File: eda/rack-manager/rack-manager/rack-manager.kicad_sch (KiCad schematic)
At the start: 49 parts, among them J1 Screw_Terminal_01x02, J10 Conn_01x04_Socket, J11 Conn_01x04_Socket, J12 Conn_01x04_Socket, J13 Conn_01x04_Socket, J14 Conn_01x04_Socket, J2 Screw_Terminal_01x02, J3 Screw_Terminal_01x02, J4 Screw_Terminal_01x02, J5 Screw_Terminal_01x02, J6 Screw_Terminal_01x02, J7 Conn_01x04_Socket, J8 Conn_01x04_Socket, J9 Conn_01x04_Socket, SW1 SW_Push, U1 ADS131M02IRUKR, U2 ADS131M02IRUKR, U3 ADS131M02IRUKR, U5 TCA9548AMRGER

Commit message: Fixed some schematic issues, added gpio expander
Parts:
- added C16, C19: 100nF, symbol Device:C_Small
- added C17, C20: 1uF, symbol Device:C_Small
- added C18: 10uF, symbol Device:C_Small
- added J15, J16: Conn_02x08_Counter_Clockwise, symbol Connector_Generic:Conn_02x08_Counter_Clockwise
- added R15: 100k, symbol Device:R
- added R16: 10k, symbol Device:R
- added U6: PCA9555PW, Package_SO:TSSOP-24_4.4x7.8mm_P0.65mm, symbol Interface_Expansion:PCA9555PW
- C13, C14, C15, C7, C8, C9: value 1nF -> 1uF
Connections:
- net I2C.SCL8 is gone; now on net I2C.SCL7: J10.1 (Pin_1)
- net I2C.SDA8 is gone; now on net I2C.SDA7: J10.2 (Pin_2)
- net +3V3: now also J10.3 (Pin_3), J11.3 (Pin_3), J12.3 (Pin_3), J13.3 (Pin_3), J14.3 (Pin_3), J7.3 (Pin_3), J8.3 (Pin_3), J9.3 (Pin_3), C16.1, C17.1, C18.2, C19.1, C20.1, R15.1, R16.1, U6.24 (VDD)
- net GND: now also C16.2, C17.2, C18.1, C19.2, C20.2, J15.10 (Pin_10), J15.11 (Pin_11), J15.12 (Pin_12), J15.13 (Pin_13), J15.14 (Pin_14), J15.15 (Pin_15), J15.16 (Pin_16), J15.9 (Pin_9), J16.10 (Pin_10), J16.11 (Pin_11), J16.12 (Pin_12), J16.13 (Pin_13), J16.14 (Pin_14), J16.15 (Pin_15), J16.16 (Pin_16), J16.9 (Pin_9), U6.12 (VSS), U6.2 (A1), U6.21 (A0), U6.3 (A2)
- net I2C.SCL6: now also J14.1 (Pin_1)
- net I2C.SCL7: no longer J14.1 (Pin_1)
- net I2C.SDA5: now also J9.2 (Pin_2)
- net I2C.SDA6: now also J14.2 (Pin_2); no longer J9.2 (Pin_2)
- net I2C.SDA7: no longer J14.2 (Pin_2)
- net at U3.10 (CS): now also U4.8 (IO17); no longer U4.22 (IO12)
- net at U1.11 (DRDY), U2.11 (DRDY), U3.11 (DRDY): now also U4.23 (I35), R15.2; no longer U4.19 (I36)
- net at U1.12 (SCLK), U2.12 (SCLK), U3.12 (SCLK): now also U4.22 (IO12); no longer U4.8 (IO17)
- net at R14.2, U4.5 (IO32), U5.19 (SCL): now also U6.22 (SCL)
- net at R13.2, U4.6 (IO33), U5.20 (SDA): now also U6.23 (SDA)
- new net: R16.2, U4.19 (I36), U6.1 (~{INT})
- new net: J16.1 (Pin_1), U6.13 (IO1_0)
- new net: J16.2 (Pin_2), U6.14 (IO1_1)
- new net: J16.3 (Pin_3), U6.15 (IO1_2)
- new net: J16.4 (Pin_4), U6.16 (IO1_3)
- new net: J16.5 (Pin_5), U6.17 (IO1_4)
- new net: J16.6 (Pin_6), U6.18 (IO1_5)
- new net: J16.7 (Pin_7), U6.19 (IO1_6)
- new net: J16.8 (Pin_8), U6.20 (IO1_7)
- new net: J15.1 (Pin_1), U6.4 (IO0_0)
- new net: J15.2 (Pin_2), U6.5 (IO0_1)
- new net: J15.3 (Pin_3), U6.6 (IO0_2)
- new net: J15.4 (Pin_4), U6.7 (IO0_3)
- new net: J15.5 (Pin_5), U6.8 (IO0_4)
- new net: J15.6 (Pin_6), U6.9 (IO0_5)
- new net: J15.7 (Pin_7), U6.10 (IO0_6)
- new net: J15.8 (Pin_8), U6.11 (IO0_7)
- no-connect marks 8 -> 0
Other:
- note added: "3v3 reservoir"
- note added: "A1=A2=A3=0 Addr = 0x20"
- note added: "A1=A2=A3=0 Addr = 0x70"
- note added: "Can't add pullup on CS1 due to IO2 needing to float on boot. To keep it uniform, there are no CS pullups for any of the chips. Instead, we pull them low in software after boot, and then issue a reset to clear any incorrect register values."
- note removed: "A1=A2=A3=0 sets the slave address of the MUX to 0x70"
- moved on the sheet: C1, C10, C11, C12, C13, C2, C3, C4, C5, C6, C7, J1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

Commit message: CAD model for mini ITX mainboard
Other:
- added sheet Analog Front-End (proposed) (analog-front-end.kicad_sch)
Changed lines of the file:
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@@
 		)
 	)
+  (sheet (at 40.0 265.0) (size 55.0 22.0) (fields_autoplaced yes)
+    (stroke (width 0.0006) (type default))
+    (fill (color 0 0 0 0.0000))
+    (property "Sheet name" "Analog Front-End (proposed)" (at 42.54 263.73 0)
+      (effects (font (size 1.27 1.27)) (justify left bottom))
+    )
+    (property "Sheet file" "analog-front-end.kicad_sch" (at 42.54 288.27 0)
+      (effects (font (size 1.27 1.27)) (justify left bottom))
+    )
+  )
 	(sheet_instances
 		(path "/"
 			(page "1")
 		)
-	)
+	    (path "/0c901832-f2ae-4e21-828e-2f1694f3c1c7" (page "2"))
+  )
 	(embedded_fonts no)
 )

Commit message: Rack manager work
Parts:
- added J17: Conn_01x04_Socket, symbol Connector:Conn_01x04_Socket
- added R17, R18, R19, R20, R21, R22, R23, R24, R25, R26, R27, R28, R29, R30, R31, R32: 10k, symbol Device:R
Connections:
- net +3V3: now also J17.3 (Pin_3), R17.1, R18.1, R19.1, R20.1, R21.1, R22.1, R23.1, R24.1, R25.1, R26.1, R27.1, R28.1, R29.1, R30.1, R31.1, R32.1
- net GND: now also J17.4 (Pin_4)
- net I2C.SCL0: now also R17.2
- net I2C.SCL1: now also R26.2
- net I2C.SCL2: now also R20.2
- net I2C.SCL3: now also R28.2
- net I2C.SCL4: now also R22.2
- net I2C.SCL5: now also R30.2
- net I2C.SCL6: now also R24.2
- net I2C.SCL7: now also R32.2
- net I2C.SDA0: now also R18.2
- net I2C.SDA1: now also R25.2
- net I2C.SDA2: now also R19.2
- net I2C.SDA3: now also R27.2
- net I2C.SDA4: now also R21.2
- net I2C.SDA5: now also R29.2
- net I2C.SDA6: now also R23.2
- net I2C.SDA7: now also R31.2
- net at R15.2, U1.11 (DRDY), U4.23 (I35): no longer U2.11 (DRDY), U3.11 (DRDY)
- net at R14.2, U4.5 (IO32), U5.19 (SCL)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: now also J17.1 (Pin_1)
- net at R13.2, U4.6 (IO33), U5.20 (SDA)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: now also J17.2 (Pin_2)
- no-connect marks 0 -> 2
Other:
- removed sheet Analog Front-End (proposed)
- moved on the sheet: C16, C17, R13, R14

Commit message: Board manager work
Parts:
- removed J15, J16: Conn_02x08_Counter_Clockwise, symbol Connector_Generic:Conn_02x08_Counter_Clockwise
- added C1, C2, C27, C28, C3: 100nF, Capacitor_SMD:C_0805_2012Metric, symbol Device:C_Small
- added C29, C30, C31, C4, C5, C6: 10uF, Capacitor_SMD:C_0805_2012Metric, symbol Device:C_Small
- added J10, J3, J6, J9: Screw_Terminal_01x02, TerminalBlock_Phoenix:TerminalBlock_Phoenix_MKDS-1-2-3.81_1x02_P3.81mm_Horizontal, symbol Connector:Screw_Terminal_01x02
- added J11: Conn_02x03_Odd_Even, Connector_IDC:IDC-Header_2x03_P2.54mm_Vertical, symbol Connector_Generic:Conn_02x03_Odd_Even
- added J12: Conn_01x02_Pin, Connector_PinHeader_1.00mm:PinHeader_1x02_P1.00mm_Vertical, symbol Connector:Conn_01x02_Pin
- added J14, J15: Conn_02x06_Counter_Clockwise, Connector_IDC:IDC-Header_2x06_P2.54mm_Vertical, symbol Connector_Generic:Conn_02x06_Counter_Clockwise
- added R15, R16: 1k, Resistor_SMD:R_0805_2012Metric, symbol Device:R
- C10: renamed from C4; footprint (none) -> Capacitor_SMD:C_0805_2012Metric
- C11: renamed from C5; footprint (none) -> Capacitor_SMD:C_0805_2012Metric
- C12: renamed from C6; footprint (none) -> Capacitor_SMD:C_0805_2012Metric
- C13: renamed from C7; footprint (none) -> Capacitor_SMD:C_0805_2012Metric
- C14: renamed from C8; footprint (none) -> Capacitor_SMD:C_0805_2012Metric
- C15: renamed from C9; footprint (none) -> Capacitor_SMD:C_0805_2012Metric
- C16: renamed from C10; footprint (none) -> Capacitor_SMD:C_0805_2012Metric
- C17: renamed from C11; footprint (none) -> Capacitor_SMD:C_0805_2012Metric
- C18: renamed from C12; footprint (none) -> Capacitor_SMD:C_0805_2012Metric
- C19: renamed from C13; footprint (none) -> Capacitor_SMD:C_0805_2012Metric
- C20: renamed from C14; footprint (none) -> Capacitor_SMD:C_0805_2012Metric
- C21: renamed from C15; footprint (none) -> Capacitor_SMD:C_0805_2012Metric
- C22: renamed from C18; footprint (none) -> Capacitor_SMD:C_0805_2012Metric
- C23: renamed from C19; footprint (none) -> Capacitor_SMD:C_0805_2012Metric
- C24: renamed from C20; footprint (none) -> Capacitor_SMD:C_0805_2012Metric
- C25: renamed from C16; footprint (none) -> Capacitor_SMD:C_0805_2012Metric
- C26: renamed from C17; footprint (none) -> Capacitor_SMD:C_0805_2012Metric
- C7: renamed from C1; footprint (none) -> Capacitor_SMD:C_0805_2012Metric
- C8: renamed from C2; footprint (none) -> Capacitor_SMD:C_0805_2012Metric
- C9: renamed from C3; footprint (none) -> Capacitor_SMD:C_0805_2012Metric
- J1, J2: footprint (none) -> TerminalBlock_Phoenix:TerminalBlock_Phoenix_MKDS-1-2-3.81_1x02_P3.81mm_Horizontal; now not fitted
- J13: renamed from J17; footprint (none) -> Connector_JST:JST_XH_B4B-XH-A_1x04_P2.50mm_Vertical; now not fitted
- J16: renamed from J7; footprint (none) -> Connector_JST:JST_XH_B4B-XH-A_1x04_P2.50mm_Vertical; now not fitted
- J17: renamed from J8; footprint (none) -> Connector_JST:JST_XH_B4B-XH-A_1x04_P2.50mm_Vertical; now not fitted
- J18: renamed from J9; footprint (none) -> Connector_JST:JST_XH_B4B-XH-A_1x04_P2.50mm_Vertical; now not fitted
- J19: renamed from J10; footprint (none) -> Connector_JST:JST_XH_B4B-XH-A_1x04_P2.50mm_Vertical; now not fitted
- J20: renamed from J11; footprint (none) -> Connector_JST:JST_XH_B4B-XH-A_1x04_P2.50mm_Vertical; now not fitted
- J21: renamed from J12; footprint (none) -> Connector_JST:JST_XH_B4B-XH-A_1x04_P2.50mm_Vertical; now not fitted
- J22: renamed from J13; footprint (none) -> Connector_JST:JST_XH_B4B-XH-A_1x04_P2.50mm_Vertical; now not fitted
- J23: renamed from J14; footprint (none) -> Connector_JST:JST_XH_B4B-XH-A_1x04_P2.50mm_Vertical; now not fitted
- J4: renamed from J3; footprint (none) -> TerminalBlock_Phoenix:TerminalBlock_Phoenix_MKDS-1-2-3.81_1x02_P3.81mm_Horizontal; now not fitted
- J5: renamed from J4; footprint (none) -> TerminalBlock_Phoenix:TerminalBlock_Phoenix_MKDS-1-2-3.81_1x02_P3.81mm_Horizontal; now not fitted
- J7: renamed from J5; footprint (none) -> TerminalBlock_Phoenix:TerminalBlock_Phoenix_MKDS-1-2-3.81_1x02_P3.81mm_Horizontal; now not fitted
- J8: renamed from J6; footprint (none) -> TerminalBlock_Phoenix:TerminalBlock_Phoenix_MKDS-1-2-3.81_1x02_P3.81mm_Horizontal; now not fitted
- R1, R10, R11, R12, R2, R3, R4, R5, R6, R7, R8, R9: footprint (none) -> Resistor_SMD:R_0805_2012Metric
- R13: renamed from R15; footprint (none) -> Resistor_SMD:R_0805_2012Metric
- R14: renamed from R16; footprint (none) -> Resistor_SMD:R_0805_2012Metric
- R17: renamed from R13; footprint (none) -> Resistor_SMD:R_0805_2012Metric
- R18: renamed from R14; footprint (none) -> Resistor_SMD:R_0805_2012Metric
- R19: renamed from R29; footprint (none) -> Resistor_SMD:R_0805_2012Metric
- R20: renamed from R25; footprint (none) -> Resistor_SMD:R_0805_2012Metric
- R21: renamed from R27; footprint (none) -> Resistor_SMD:R_0805_2012Metric
- R22: renamed from R31; footprint (none) -> Resistor_SMD:R_0805_2012Metric
- R23: renamed from R30; footprint (none) -> Resistor_SMD:R_0805_2012Metric
- R24: renamed from R26; footprint (none) -> Resistor_SMD:R_0805_2012Metric
- R25: renamed from R28; footprint (none) -> Resistor_SMD:R_0805_2012Metric
- R26: renamed from R32; footprint (none) -> Resistor_SMD:R_0805_2012Metric
- R27: renamed from R19; footprint (none) -> Resistor_SMD:R_0805_2012Metric
- R28: renamed from R18; footprint (none) -> Resistor_SMD:R_0805_2012Metric
- R29: renamed from R21; footprint (none) -> Resistor_SMD:R_0805_2012Metric
- R30: renamed from R23; footprint (none) -> Resistor_SMD:R_0805_2012Metric
- R31: renamed from R20; footprint (none) -> Resistor_SMD:R_0805_2012Metric
- R32: renamed from R17; footprint (none) -> Resistor_SMD:R_0805_2012Metric
- R33: renamed from R22; footprint (none) -> Resistor_SMD:R_0805_2012Metric
- R34: renamed from R24; footprint (none) -> Resistor_SMD:R_0805_2012Metric
- SW1: footprint (none) -> Button_Switch_SMD:SW_Push_SPST_NO_Alps_SKRK
- U1, U2, U3: footprint WQFN20_ADS131_TEX -> Package_DFN_QFN:WQFN-20-1EP_3x3mm_P0.4mm_EP1.7x1.7mm
- U4: footprint (none) -> rack-manager:WT32-ETH01; now not fitted
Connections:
- net +3V3: now also C1.2, C2.2, C27.2, C28.2, C29.2, C3.2, C30.2, C31.2, C4.2, C5.2, C6.2, J11.1 (Pin_1), J14.5 (Pin_5), J14.6 (Pin_6), J15.5 (Pin_5), J15.6 (Pin_6), J3.2 (Pin_2), J6.2 (Pin_2), J9.2 (Pin_2)
- net +5V: now also J10.2 (Pin_2)
- net GND: now also U4.14 (GND), U4.23 (GND), C1.1, C2.1, C27.1, C28.1, C29.1, C3.1, C30.1, C31.1, C4.1, C5.1, C6.1, J10.1 (Pin_1), J11.2 (Pin_2), J14.7 (Pin_7), J14.8 (Pin_8), J15.7 (Pin_7), J15.8 (Pin_8), J3.1 (Pin_1), J6.1 (Pin_1), J9.1 (Pin_1), R15.1, R16.1; no longer U4.17 (GND), U4.26 (GND)
- net at C10.1, R8.2: now also U2.3 (AIN1N); no longer U2.4 (AIN1P)
- net at C8.1, R4.2: now also U1.3 (AIN1N); no longer U1.4 (AIN1P)
- net at C8.2, R3.2: now also U1.4 (AIN1P); no longer U1.3 (AIN1N)
- net at C11.2, R9.2: now also U3.2 (AIN0N); no longer U3.1 (AIN0P)
- net at U1.12 (SCLK), U2.12 (SCLK), U3.12 (SCLK): now also U4.18 (IO12); no longer U4.22 (IO12)
- net at U1.13 (DOUT), U2.13 (DOUT), U3.13 (DOUT): now also U4.22 (I39); no longer U4.18 (I39)
- net at U1.15 (CLKIN), U2.15 (CLKIN), U3.15 (CLKIN): now also U4.19 (IO14); no longer U4.21 (IO14)
- net at C11.1, R10.2: now also U3.1 (AIN0P); no longer U3.2 (AIN0N)
- net at C12.2, R11.2: now also U3.4 (AIN1P); no longer U3.3 (AIN1N)
- net at C12.1, R12.2: now also U3.3 (AIN1N); no longer U3.4 (AIN1P)
- net at SW1.2, U4.1 (CLK_EN), U4.4 (ESP32_EN)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: now also J11.3 (Pin_3)
- net at C10.2, R7.2: now also U2.4 (AIN1P); no longer U2.3 (AIN1N)
- net at R13.2, U1.11 (DRDY): now also U4.17 (I35); no longer U4.23 (I35)
- net at U4.13 (Link): now also J12.2 (Pin_2)
- net at U4.15 (IO2): now also U1.10 (CS)
- net at U4.16 (IO4): now also U2.10 (CS)
- net at R14.2, U6.1 (~{INT}): now also U4.21 (I36); no longer U4.19 (I36)
- net at U4.24 (IO0): now also J11.5 (Pin_5); no longer U2.10 (CS)
- net at U4.25 (IO3): now also J11.4 (Pin_4); no longer U1.10 (CS)
- net GPIO10: now reaches U6.13 (IO1_0)
- net GPIO10: now also J14.1 (Pin_1)
- net GPIO11: now reaches U6.14 (IO1_1)
- net GPIO11: now also J14.2 (Pin_2)
- net GPIO12: now reaches U6.15 (IO1_2)
- net GPIO12: now also J14.3 (Pin_3)
- net GPIO13: now reaches U6.16 (IO1_3)
- net GPIO13: now also J14.4 (Pin_4)
- net GPIO14: now reaches U6.17 (IO1_4)
- net GPIO14: now also J14.12 (Pin_12)
- net GPIO15: now reaches U6.18 (IO1_5)
- net GPIO15: now also J14.11 (Pin_11)
- net GPIO16: now reaches U6.19 (IO1_6)
- net GPIO16: now also J14.10 (Pin_10)
- net GPIO17: now reaches U6.20 (IO1_7)
- net GPIO17: now also J14.9 (Pin_9)
- net at C9.1, R6.2: now also U2.1 (AIN0P); no longer U2.2 (AIN0N)
- net at C9.2, R5.2: now also U2.2 (AIN0N); no longer U2.1 (AIN0P)
- net at C7.1, R2.2: now also U1.1 (AIN0P); no longer U1.2 (AIN0N)
- net at C7.2, R1.2: now also U1.2 (AIN0N); no longer U1.1 (AIN0P)
- net GPIO00: now reaches U6.4 (IO0_0)
- net GPIO00: now also J15.1 (Pin_1)
- net GPIO01: now reaches U6.5 (IO0_1)
- net GPIO01: now also J15.2 (Pin_2)
- net GPIO02: now reaches U6.6 (IO0_2)
- net GPIO02: now also J15.3 (Pin_3)
- net GPIO03: now reaches U6.7 (IO0_3)
- net GPIO03: now also J15.4 (Pin_4)
- net GPIO04: now reaches U6.8 (IO0_4)
- net GPIO04: now also J15.12 (Pin_12)
- net GPIO05: now reaches U6.9 (IO0_5)
- net GPIO05: now also J15.11 (Pin_11)
- net GPIO06: now reaches U6.10 (IO0_6)
- net GPIO06: now also J15.10 (Pin_10)
- net GPIO07: now reaches U6.11 (IO0_7)
- net GPIO07: now also J15.9 (Pin_9)
- new net: J11.6 (Pin_6), U4.26 (IO1)
- new net: J12.1 (Pin_1), R15.2, R16.2
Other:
- note removed: "3v3 reservoir"
- moved on the sheet: R17, R18, SW1

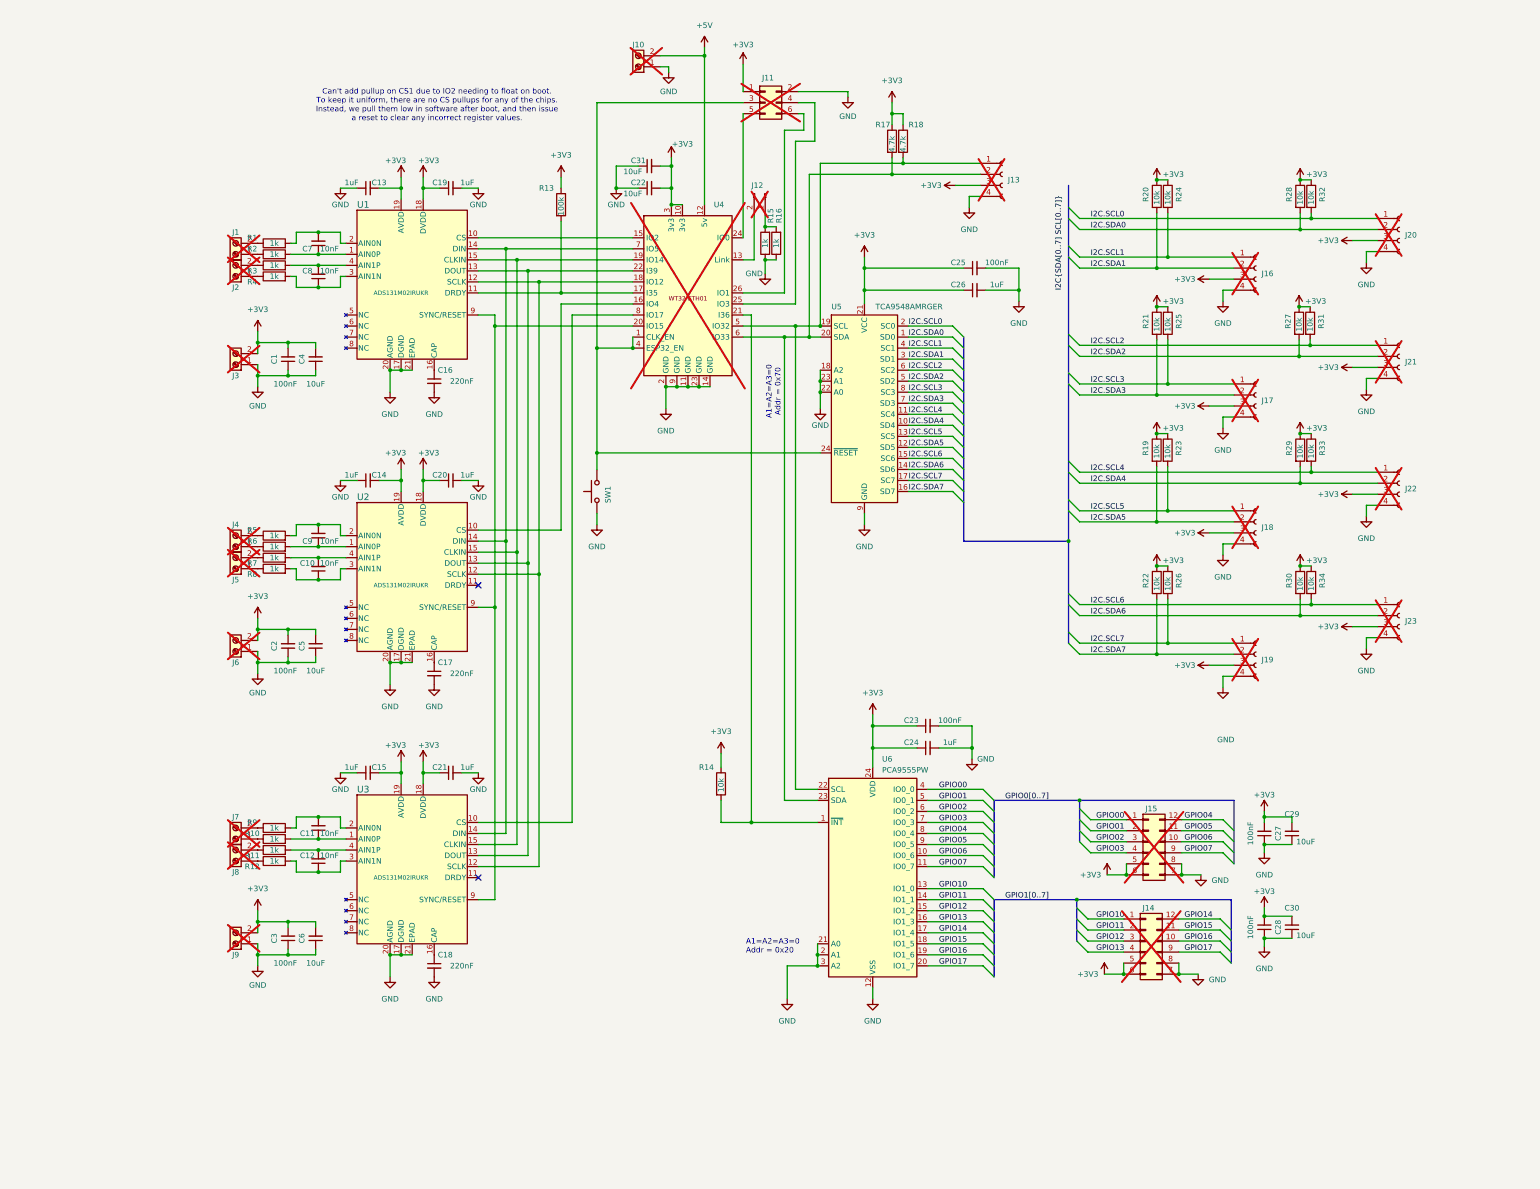
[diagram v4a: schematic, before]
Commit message: Rack manager PCB component placement
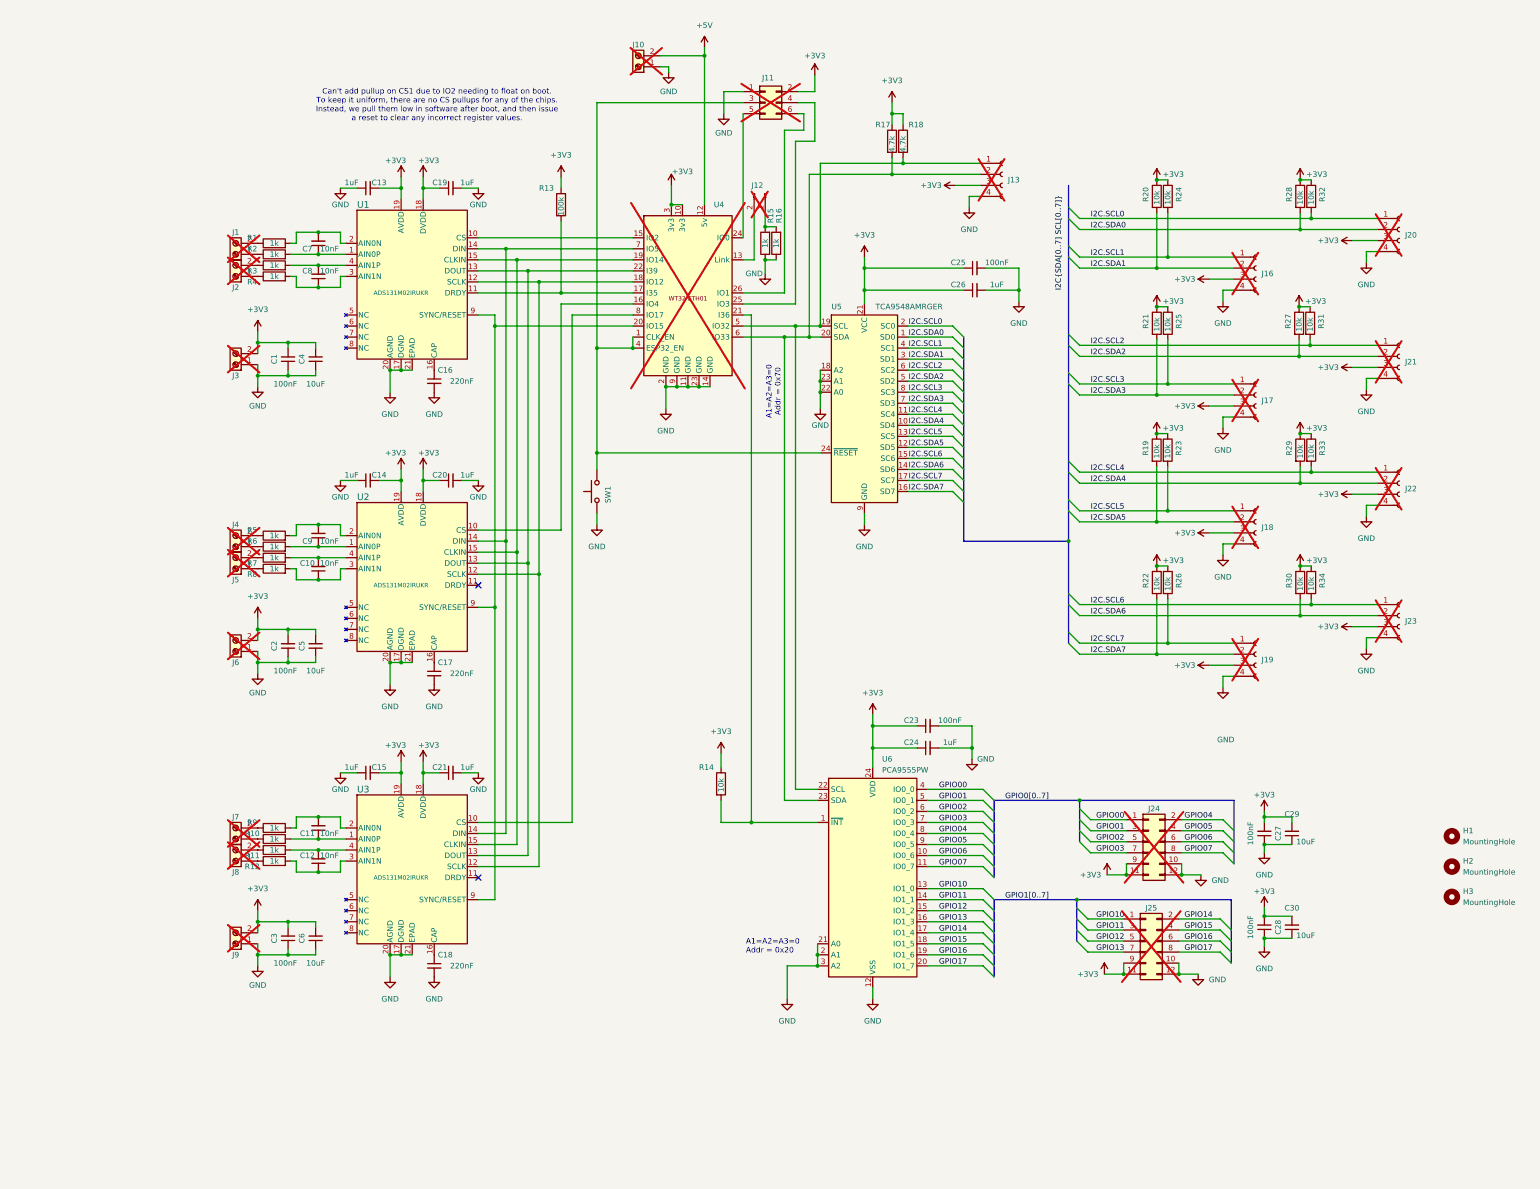
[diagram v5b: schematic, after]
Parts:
- removed C22, C31: 10uF, Capacitor_SMD:C_0805_2012Metric, symbol Device:C_Small
- removed J14, J15: Conn_02x06_Counter_Clockwise, Connector_IDC:IDC-Header_2x06_P2.54mm_Vertical, symbol Connector_Generic:Conn_02x06_Counter_Clockwise
- added H1, H2, H3: MountingHole, MountingHole:MountingHole_4.3mm_M4_ISO14580_Pad_TopBottom, symbol Mechanical:MountingHole
- added J24, J25: Conn_02x06_Odd_Even, Connector_IDC:IDC-Header_2x06_P2.54mm_Vertical, symbol Connector_Generic:Conn_02x06_Odd_Even
- C1, C2, C23, C25, C27, C28, C3: footprint Capacitor_SMD:C_0805_2012Metric -> Capacitor_SMD:C_0603_1608Metric; LCSC (none) -> C14663
- C10, C11, C12, C7, C8, C9: footprint Capacitor_SMD:C_0805_2012Metric -> Capacitor_SMD:C_0603_1608Metric; LCSC (none) -> C57112
- C13, C14, C15, C19, C20, C21, C24, C26: footprint Capacitor_SMD:C_0805_2012Metric -> Capacitor_SMD:C_0603_1608Metric; LCSC (none) -> C15849
- C16, C17, C18: footprint Capacitor_SMD:C_0805_2012Metric -> Capacitor_SMD:C_0603_1608Metric; LCSC (none) -> C21120
- C29, C30, C4, C5, C6: footprint Capacitor_SMD:C_0805_2012Metric -> Capacitor_SMD:C_0603_1608Metric; LCSC (none) -> C19702
- R1, R10, R11, R12, R15, R16, R2, R3, R4, R5, R6, R7, R8, R9: footprint Resistor_SMD:R_0805_2012Metric -> Resistor_SMD:R_0603_1608Metric; LCSC (none) -> C21190
- R13: footprint Resistor_SMD:R_0805_2012Metric -> Resistor_SMD:R_0603_1608Metric; LCSC (none) -> C25803
- R14, R19, R20, R21, R22, R23, R24, R25, R26, R27, R28, R29, R30, R31, R32, R33, R34: footprint Resistor_SMD:R_0805_2012Metric -> Resistor_SMD:R_0603_1608Metric; LCSC (none) -> C25804
- R17, R18: footprint Resistor_SMD:R_0805_2012Metric -> Resistor_SMD:R_0603_1608Metric; LCSC (none) -> C23162
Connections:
- net +3V3: now also J11.2 (Pin_2), J24.11 (Pin_11), J24.9 (Pin_9), J25.11 (Pin_11), J25.9 (Pin_9); no longer J11.1 (Pin_1)
- net GND: now also J11.1 (Pin_1), J24.10 (Pin_10), J24.12 (Pin_12), J25.10 (Pin_10), J25.12 (Pin_12); no longer J11.2 (Pin_2)
- net GPIO00: now also J24.1 (Pin_1)
- net GPIO01: now also J24.3 (Pin_3)
- net GPIO02: now also J24.5 (Pin_5)
- net GPIO03: now also J24.7 (Pin_7)
- net GPIO04: now also J24.2 (Pin_2)
- net GPIO05: now also J24.4 (Pin_4)
- net GPIO06: now also J24.6 (Pin_6)
- net GPIO07: now also J24.8 (Pin_8)
- net GPIO10: now also J25.1 (Pin_1)
- net GPIO11: now also J25.3 (Pin_3)
- net GPIO12: now also J25.5 (Pin_5)
- net GPIO13: now also J25.7 (Pin_7)
- net GPIO14: now also J25.2 (Pin_2)
- net GPIO15: now also J25.4 (Pin_4)
- net GPIO16: now also J25.6 (Pin_6)
- net GPIO17: now also J25.8 (Pin_8)
